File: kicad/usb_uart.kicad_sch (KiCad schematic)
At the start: 10 parts, among them Q3 DMN2004WK-7, U5 CP2102N-Axx-xQFN28

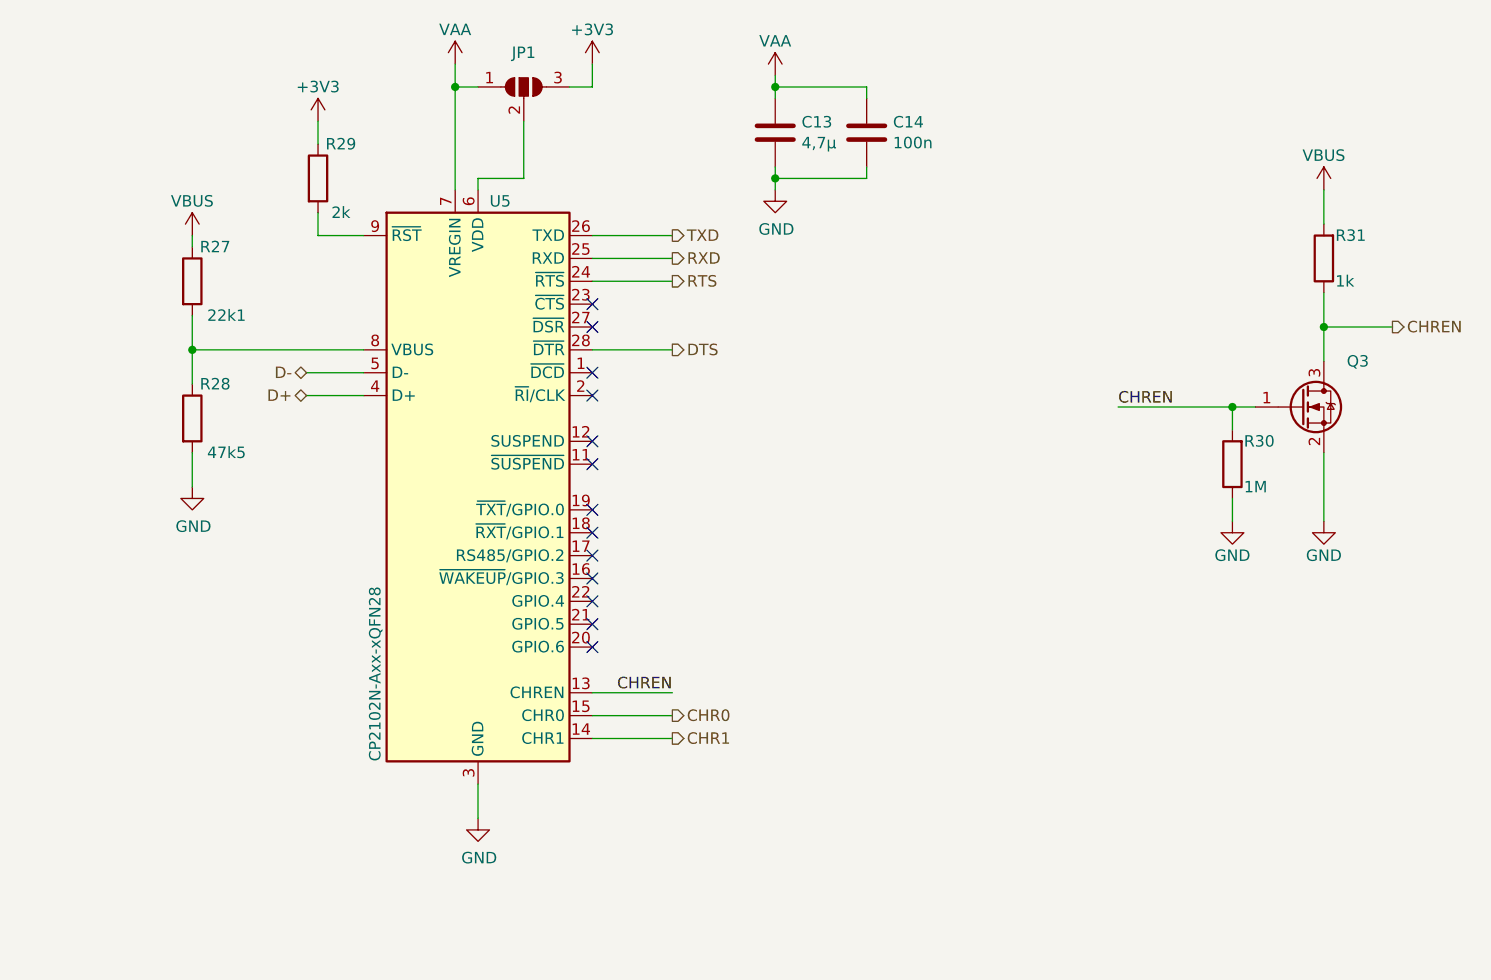
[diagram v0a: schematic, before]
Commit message: refactor KiCAD Project to v6
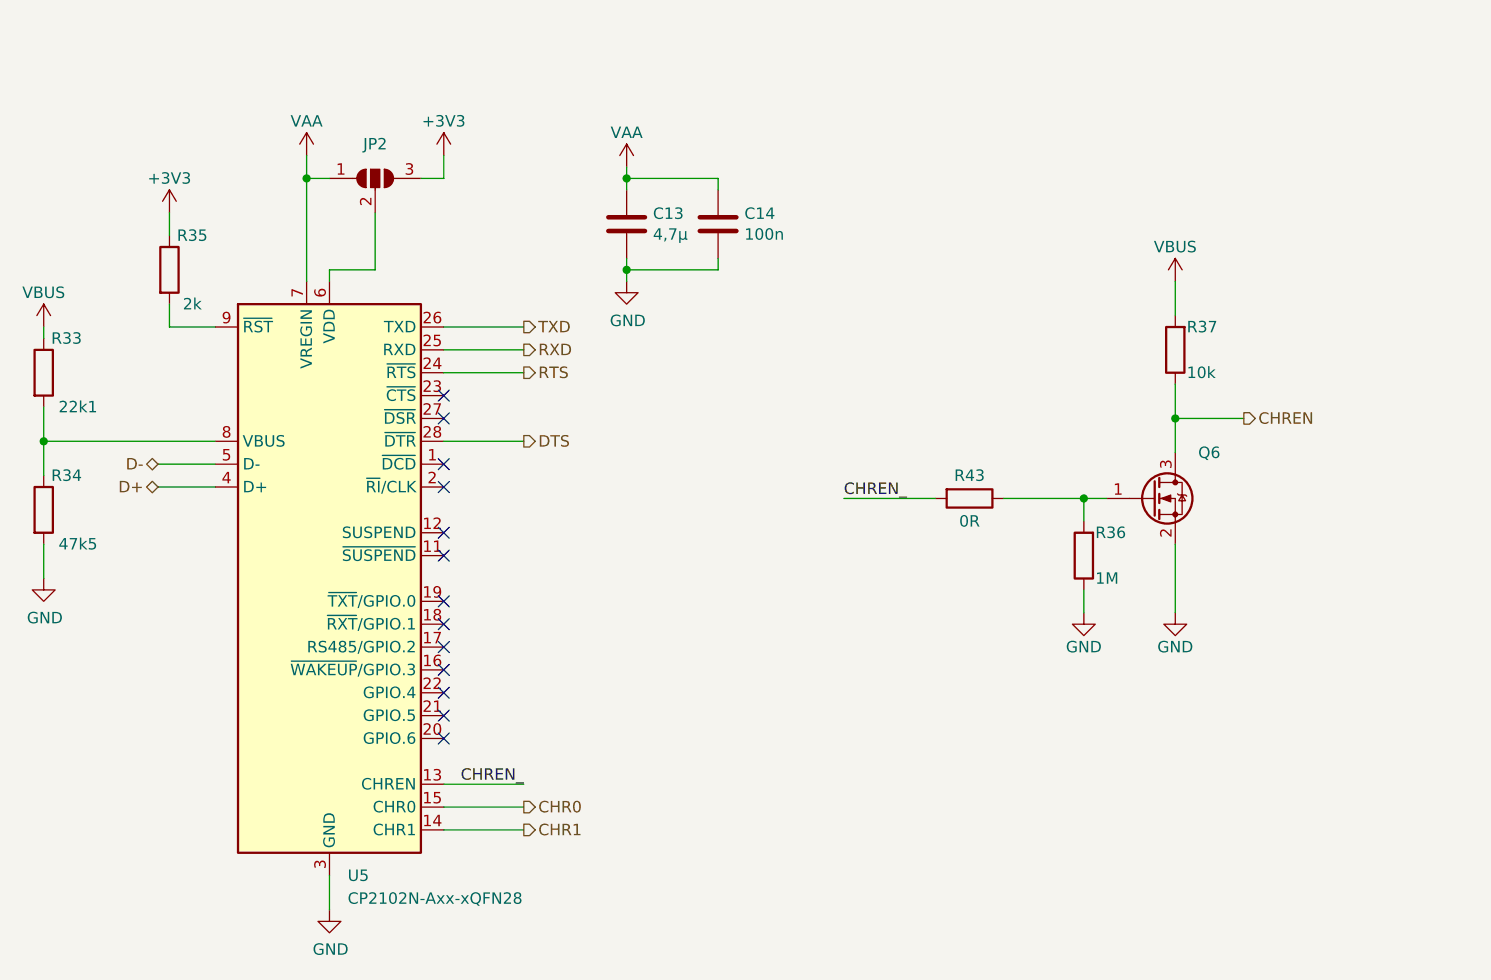
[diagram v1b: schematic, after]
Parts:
- removed JP1: SolderJumper_3_Open, Jumper:SolderJumper-3_P1.3mm_Open_Pad1.0x1.5mm_NumberLabels, symbol Jumper:SolderJumper_3_Open
- removed Q3: DMN2004WK-7, Package_TO_SOT_SMD:SOT-323_SC-70, symbol z_ic:DMN2004WK-7
- removed R27: 22k1, Resistor_SMD:R_0603_1608Metric, symbol Device:R
- removed R28: 47k5, Resistor_SMD:R_0603_1608Metric, symbol Device:R
- removed R29: 2k, Resistor_SMD:R_0603_1608Metric, symbol Device:R
- removed R30: 1M, Resistor_SMD:R_0603_1608Metric, symbol Device:R
- removed R31: 1k, Resistor_SMD:R_0603_1608Metric, symbol Device:R
- added JP2: SolderJumper_3_Open, Jumper:SolderJumper-3_P1.3mm_Open_Pad1.0x1.5mm_NumberLabels, symbol Jumper:SolderJumper_3_Open
- added Q6: DMN2004WK-7, Package_TO_SOT_SMD:SOT-323_SC-70, symbol z_ic:DMN2004WK-7
- added R33: 22k1, Resistor_SMD:R_0603_1608Metric, symbol Device:R
- added R34: 47k5, Resistor_SMD:R_0603_1608Metric, symbol Device:R
- added R35: 2k, Resistor_SMD:R_0603_1608Metric, symbol Device:R
- added R36: 1M, Resistor_SMD:R_0603_1608Metric, symbol Device:R
- added R37: 10k, Resistor_SMD:R_0603_1608Metric, symbol Device:R
- added R43: 0R, Resistor_SMD:R_0603_1608Metric, symbol Device:R
- U5: Digikey (none) -> 336-5889-ND
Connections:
- net +3V3: now also JP2.3 (B), R35.1
- net CHREN: now also Q6.3 (D), R37.1; no longer U5.13 (CHREN)
- net GND: now also Q6.2 (S), R34.2, R36.1
- net VAA: now also JP2.1 (A)
- net VBUS: now also R33.1, R37.2
- net at U5.8 (VBUS): now also R33.2, R34.1
- net at U5.9 (~{RST}): now also R35.2
- net at U5.6 (VDD): now also JP2.2 (C)
- new net: Q6.1 (G), R36.2, R43.1
- new net CHREN_: R43.2, U5.13 (CHREN)

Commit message: route complete pcb
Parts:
- removed JP2: SolderJumper_3_Open, Jumper:SolderJumper-3_P1.3mm_Open_Pad1.0x1.5mm_NumberLabels, symbol Jumper:SolderJumper_3_Open
- added R38: 0R, Resistor_SMD:R_0603_1608Metric, symbol Device:R
- renumbered Q6 to Q5, R33 to R35, R34 to R36, R35 to R37, R43 to R39, R36 to R40, R37 to R41
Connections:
- net +3V3: now also R38.1
- net at U5.6 (VDD): now also R38.2
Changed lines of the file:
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@@
   (junction (at 154.94 68.58) (diameter 0) (color 0 0 0 0)
-  )
-  (junction (at 119.38 58.42) (diameter 0) (color 0 0 0 0)
   )
   (junction (at 154.94 58.42) (diameter 0) (color 0 0 0 0)
@@
     (stroke (width 0) (type default) (color 0 0 0 0))
   )
-  (wire (pts (xy 119.38 58.42) (xy 119.38 69.85))
+  (wire (pts (xy 119.38 55.88) (xy 119.38 69.85))
     (stroke (width 0) (type default) (color 0 0 0 0))
   )
@@
     (stroke (width 0) (type default) (color 0 0 0 0))
   )
-  (wire (pts (xy 127 62.23) (xy 127 68.58))
-    (stroke (width 0) (type default) (color 0 0 0 0))
-  )
   (wire (pts (xy 109.22 90.17) (xy 102.87 90.17))
     (stroke (width 0) (type default) (color 0 0 0 0))
@@
     (stroke (width 0) (type default) (color 0 0 0 0))
   )
-  (wire (pts (xy 119.38 55.88) (xy 119.38 58.42))
-    (stroke (width 0) (type default) (color 0 0 0 0))
-  )
   (wire (pts (xy 179.07 93.98) (xy 189.23 93.98))
     (stroke (width 0) (type default) (color 0 0 0 0))
@@
     (stroke (width 0) (type default) (color 0 0 0 0))
   )
-  (wire (pts (xy 121.92 69.85) (xy 121.92 68.58))
-    (stroke (width 0) (type default) (color 0 0 0 0))
-  )
-  (wire (pts (xy 134.62 58.42) (xy 134.62 55.88))
-    (stroke (width 0) (type default) (color 0 0 0 0))
-  )
-  (wire (pts (xy 121.92 68.58) (xy 127 68.58))
+  (wire (pts (xy 121.92 69.85) (xy 121.92 67.31))
+    (stroke (width 0) (type default) (color 0 0 0 0))
+  )
+  (wire (pts (xy 129.54 55.88) (xy 129.54 58.42))
     (stroke (width 0) (type default) (color 0 0 0 0))
   )
@@
     (stroke (width 0) (type default) (color 0 0 0 0))
   )
+  (wire (pts (xy 129.54 66.04) (xy 129.54 67.31))
+    (stroke (width 0) (type default) (color 0 0 0 0))
+  )
   (wire (pts (xy 215.9 85.09) (xy 223.52 85.09))
     (stroke (width 0) (type default) (color 0 0 0 0))
   )
-  (wire (pts (xy 119.38 58.42) (xy 121.92 58.42))
-    (stroke (width 0) (type default) (color 0 0 0 0))
-  )
   (wire (pts (xy 154.94 68.58) (xy 165.1 68.58))
     (stroke (width 0) (type default) (color 0 0 0 0))
   )
-  (wire (pts (xy 132.08 58.42) (xy 134.62 58.42))
-    (stroke (width 0) (type default) (color 0 0 0 0))
-  )
   (wire (pts (xy 134.62 128.27) (xy 143.51 128.27))
     (stroke (width 0) (type default) (color 0 0 0 0))
@@
   )
   (wire (pts (xy 196.85 93.98) (xy 205.74 93.98))
+    (stroke (width 0) (type default) (color 0 0 0 0))
+  )
+  (wire (pts (xy 121.92 67.31) (xy 129.54 67.31))
     (stroke (width 0) (type default) (color 0 0 0 0))
   )
@@
   (symbol (lib_id "Device:R") (at 205.74 100.33 180) (unit 1)
     (in_bom yes) (on_board yes)
-    (property "Reference" "R36" (id 0) (at 207.01 97.79 0)
+    (property "Reference" "R40" (id 0) (at 207.01 97.79 0)
       (effects (font (size 1.27 1.27)) (justify right))
     )
@@
   (symbol (lib_id "power:GND") (at 90.17 102.87 0) (unit 1)
     (in_bom yes) (on_board yes)
-    (property "Reference" "#PWR0165" (id 0) (at 90.17 109.22 0)
+    (property "Reference" "#PWR059" (id 0) (at 90.17 109.22 0)
       (effects (font (size 1.27 1.27)) hide)
     )
@@
   (symbol (lib_id "Device:R") (at 90.17 95.25 0) (unit 1)
     (in_bom yes) (on_board yes)
-    (property "Reference" "R34" (id 0) (at 92.71 91.44 0))
+    (property "Reference" "R36" (id 0) (at 92.71 91.44 0))
     (property "Value" "47k5" (id 1) (at 93.98 99.06 0))
     (property "Footprint" "Resistor_SMD:R_0603_1608Metric" (id 2) (at 88.392 95.25 90)
@@
   (symbol (lib_id "power:VAA") (at 154.94 57.15 0) (unit 1)
     (in_bom yes) (on_board yes)
-    (property "Reference" "#PWR0169" (id 0) (at 154.94 60.96 0)
+    (property "Reference" "#PWR064" (id 0) (at 154.94 60.96 0)
       (effects (font (size 1.27 1.27)) hide)
     )
@@
   (symbol (lib_id "z_ic:DMN2004WK-7") (at 213.36 93.98 0) (unit 1)
     (in_bom yes) (on_board yes)
-    (property "Reference" "Q6" (id 0) (at 218.44 88.9 0)
+    (property "Reference" "Q5" (id 0) (at 218.44 88.9 0)
       (effects (font (size 1.27 1.27)) (justify left))
     )
@@
   (symbol (lib_id "power:GND") (at 154.94 69.85 0) (unit 1)
     (in_bom yes) (on_board yes)
-    (property "Reference" "#PWR0167" (id 0) (at 154.94 76.2 0)
+    (property "Reference" "#PWR065" (id 0) (at 154.94 76.2 0)
       (effects (font (size 1.27 1.27)) hide)
     )
@@
     (pin "1")
   )
+  (symbol (lib_id "Device:R") (at 129.54 62.23 0) (unit 1)
+    (in_bom yes) (on_board yes)
+    (property "Reference" "R38" (id 0) (at 127 62.23 90))
+    (property "Value" "0R" (id 1) (at 132.08 62.23 90))
+    (property "Footprint" "Resistor_SMD:R_0603_1608Metric" (id 2) (at 127.762 62.23 90)
+      (effects (font (size 1.27 1.27)) hide)
+    )
+    (property "Datasheet" "~" (id 3) (at 129.54 62.23 0)
+      (effects (font (size 1.27 1.27)) hide)
+    )
+    (property "Digikey" "541-0.0SBCT-ND" (id 4) (at 129.54 62.23 0)
+      (effects (font (size 1.27 1.27)) hide)
+    )
+    (pin "1")
+    (pin "2")
+  )
   (symbol (lib_id "power:GND") (at 205.74 106.68 0) (unit 1)
     (in_bom yes) (on_board yes)
-    (property "Reference" "#PWR0172" (id 0) (at 205.74 113.03 0)
+    (property "Reference" "#PWR066" (id 0) (at 205.74 113.03 0)
       (effects (font (size 1.27 1.27)) hide)
     )
@@
   (symbol (lib_id "Device:R") (at 104.14 68.58 0) (unit 1)
     (in_bom yes) (on_board yes)
-    (property "Reference" "R35" (id 0) (at 106.68 64.77 0))
+    (property "Reference" "R37" (id 0) (at 106.68 64.77 0))
     (property "Value" "2k" (id 1) (at 106.68 72.39 0))
     (property "Footprint" "Resistor_SMD:R_0603_1608Metric" (id 2) (at 102.362 68.58 90)
@@
   (symbol (lib_id "power:VBUS") (at 90.17 74.93 0) (unit 1)
     (in_bom yes) (on_board yes)
-    (property "Reference" "#PWR0166" (id 0) (at 90.17 78.74 0)
+    (property "Reference" "#PWR058" (id 0) (at 90.17 78.74 0)
       (effects (font (size 1.27 1.27)) hide)
     )
@@
   (symbol (lib_id "power:GND") (at 215.9 106.68 0) (unit 1)
     (in_bom yes) (on_board yes)
-    (property "Reference" "#PWR0171" (id 0) (at 215.9 113.03 0)
+    (property "Reference" "#PWR068" (id 0) (at 215.9 113.03 0)
       (effects (font (size 1.27 1.27)) hide)
     )
@@
   (symbol (lib_id "power:+3V3") (at 104.14 62.23 0) (unit 1)
     (in_bom yes) (on_board yes)
-    (property "Reference" "#PWR0162" (id 0) (at 104.14 66.04 0)
+    (property "Reference" "#PWR060" (id 0) (at 104.14 66.04 0)
       (effects (font (size 1.27 1.27)) hide)
     )
@@
   (symbol (lib_id "power:VBUS") (at 215.9 69.85 0) (unit 1)
     (in_bom yes) (on_board yes)
-    (property "Reference" "#PWR0170" (id 0) (at 215.9 73.66 0)
+    (property "Reference" "#PWR067" (id 0) (at 215.9 73.66 0)
       (effects (font (size 1.27 1.27)) hide)
     )
@@
     (pin "1")
   )
-  (symbol (lib_id "Jumper:SolderJumper_3_Open") (at 127 58.42 0) (unit 1)
-    (in_bom yes) (on_board yes) (fields_autoplaced)
-    (property "Reference" "JP2" (id 0) (at 127 54.61 0))
-    (property "Value" "SolderJumper_3_Open" (id 1) (at 127 54.61 0)
-      (effects (font (size 1.27 1.27)) hide)
-    )
-    (property "Footprint" "Jumper:SolderJumper-3_P1.3mm_Open_Pad1.0x1.5mm_NumberLabels" (id 2) (at 127 58.42 0)
-      (effects (font (size 1.27 1.27)) hide)
-    )
-    (property "Datasheet" "~" (id 3) (at 127 58.42 0)
-      (effects (font (size 1.27 1.27)) hide)
-    )
-    (property "Digikey" "-" (id 4) (at 127 58.42 0)
-      (effects (font (size 1.27 1.27)) hide)
-    )
-    (pin "1")
-    (pin "2")
-    (pin "3")
-  )
   (symbol (lib_id "Device:R") (at 215.9 77.47 180) (unit 1)
     (in_bom yes) (on_board yes)
-    (property "Reference" "R37" (id 0) (at 217.17 74.93 0)
+    (property "Reference" "R41" (id 0) (at 217.17 74.93 0)
       (effects (font (size 1.27 1.27)) (justify right))
     )
@@
     (pin "2")
   )
-  (symbol (lib_id "power:+3V3") (at 134.62 55.88 0) (unit 1)
-    (in_bom yes) (on_board yes)
-    (property "Reference" "#PWR0163" (id 0) (at 134.62 59.69 0)
-      (effects (font (size 1.27 1.27)) hide)
-    )
-    (property "Value" "+3V3" (id 1) (at 134.62 52.07 0))
-    (property "Footprint" "" (id 2) (at 134.62 55.88 0)
-      (effects (font (size 1.27 1.27)) hide)
-    )
-    (property "Datasheet" "" (id 3) (at 134.62 55.88 0)
+  (symbol (lib_id "power:+3V3") (at 129.54 55.88 0) (unit 1)
+    (in_bom yes) (on_board yes)
+    (property "Reference" "#PWR063" (id 0) (at 129.54 59.69 0)
+      (effects (font (size 1.27 1.27)) hide)
+    )
+    (property "Value" "+3V3" (id 1) (at 129.54 52.07 0))
+    (property "Footprint" "" (id 2) (at 129.54 55.88 0)
+      (effects (font (size 1.27 1.27)) hide)
+    )
+    (property "Datasheet" "" (id 3) (at 129.54 55.88 0)
       (effects (font (size 1.27 1.27)) hide)
     )
@@
   (symbol (lib_id "power:VAA") (at 119.38 55.88 0) (unit 1)
     (in_bom yes) (on_board yes)
-    (property "Reference" "#PWR0164" (id 0) (at 119.38 59.69 0)
+    (property "Reference" "#PWR061" (id 0) (at 119.38 59.69 0)
       (effects (font (size 1.27 1.27)) hide)
     )
@@
   (symbol (lib_id "Device:R") (at 193.04 93.98 270) (unit 1)
     (in_bom yes) (on_board yes)
-    (property "Reference" "R43" (id 0) (at 193.04 91.44 90))
+    (property "Reference" "R39" (id 0) (at 193.04 91.44 90))
     (property "Value" "0R" (id 1) (at 193.04 96.52 90))
     (property "Footprint" "Resistor_SMD:R_0603_1608Metric" (id 2) (at 193.04 92.202 90)
@@
   (symbol (lib_id "power:GND") (at 121.92 139.7 0) (unit 1)
     (in_bom yes) (on_board yes)
-    (property "Reference" "#PWR0168" (id 0) (at 121.92 146.05 0)
+    (property "Reference" "#PWR062" (id 0) (at 121.92 146.05 0)
       (effects (font (size 1.27 1.27)) hide)
     )
@@
   (symbol (lib_id "Device:R") (at 90.17 80.01 0) (unit 1)
     (in_bom yes) (on_board yes)
-    (property "Reference" "R33" (id 0) (at 92.71 76.2 0))
+    (property "Reference" "R35" (id 0) (at 92.71 76.2 0))
     (property "Value" "22k1" (id 1) (at 93.98 83.82 0))
     (property "Footprint" "Resistor_SMD:R_0603_1608Metric" (id 2) (at 88.392 80.01 90)

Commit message: rework pcb
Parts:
- removed C13: 4,7µ, Capacitor_SMD:C_0603_1608Metric, symbol Device:C
- removed C14: 100n, Capacitor_SMD:C_0603_1608Metric, symbol Device:C
- removed Q5: DMN2004WK-7, Package_TO_SOT_SMD:SOT-323_SC-70, symbol z_ic:DMN2004WK-7
- removed R35: 22k1, Resistor_SMD:R_0603_1608Metric, symbol Device:R
- removed R36: 47k5, Resistor_SMD:R_0603_1608Metric, symbol Device:R
- removed R37: 2k, Resistor_SMD:R_0603_1608Metric, symbol Device:R
- removed R38, R39: 0R, Resistor_SMD:R_0603_1608Metric, symbol Device:R
- removed R40: 1M, Resistor_SMD:R_0603_1608Metric, symbol Device:R
- removed R41: 10k, Resistor_SMD:R_0603_1608Metric, symbol Device:R
- removed U5: CP2102N-Axx-xQFN28, Package_DFN_QFN:QFN-28-1EP_5x5mm_P0.5mm_EP3.35x3.35mm, symbol Interface_USB:CP2102N-Axx-xQFN28
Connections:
- no-connect marks 13 -> 0
